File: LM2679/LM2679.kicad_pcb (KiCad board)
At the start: 2 copper layers, 61 x 35.6 mm, 15 parts, among them J1 - INPUT +, J2 + OUTPUT -, U1 LM2679SX-5.0/NOPB

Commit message: Updates to schematic and PCB
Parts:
- J1: value - INPUT + -> INPUT
- J2: value + OUTPUT - -> OUTPUT
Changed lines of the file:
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@@
   )
   (setup
-    (last_trace_width 1)
+    (last_trace_width 0.25)
     (user_trace_width 0.1)
     (user_trace_width 0.2)
@@
     (add_net "Net-(R1-Pad1)")
   )
+  (module Inductor_SMD:L_Bourns_SRP1245A (layer Front)
+    (at 154.686 83.058)
+    (descr "Bourns SRP1245A series SMD inductor http://www.bourns.com/docs/Product-Datasheets/SRP1245A.pdf")
+    (tags "Bourns SRP1245A SMD inductor")
+    (attr smd)
+    (fp_text reference L1 (at 0 7.366) (layer F.SilkS)
+      (effects (font (size 1 1) (thickness 0.15)))
+    )
+    (fp_text value "10µH 10A" (at 0 1.016) (layer F.Fab)
+      (effects (font (size 1 1) (thickness 0.15)))
+    )
+    (fp_line (start 6.45 2.8) (end 6.45 5.7) (layer F.SilkS) (width 0.12))
+    (fp_line (start -6.45 2.8) (end -6.45 5.7) (layer F.SilkS) (width 0.12))
+    (fp_line (start 5.75 6.5) (end -5.75 6.5) (layer F.CrtYd) (width 0.05))
+    (fp_line (start -5.75 -6.5) (end 5.75 -6.5) (layer F.CrtYd) (width 0.05))
+    (fp_line (start 6.45 -5.7) (end 6.45 -2.8) (layer F.SilkS) (width 0.12))
+    (fp_line (start 5.75 6.4) (end -5.75 6.4) (layer F.SilkS) (width 0.12))
+    (fp_line (start -6.45 -5.75) (end -6.45 -2.8) (layer F.SilkS) (width 0.12))
+    (fp_line (start -5.75 -6.4) (end 5.75 -6.4) (layer F.SilkS) (width 0.12))
+    (fp_line (start 6.3 -5.7) (end 6.3 5.7) (layer F.Fab) (width 0.1))
+    (fp_line (start 5.75 6.25) (end -5.75 6.25) (layer F.Fab) (width 0.1))
+    (fp_line (start -6.3 -5.75) (end -6.3 5.7) (layer F.Fab) (width 0.1))
+    (fp_line (start -5.75 -6.25) (end 5.75 -6.25) (layer F.Fab) (width 0.1))
+    (fp_line (start 8.001 2.7568) (end 6.55 2.75) (layer F.CrtYd) (width 0.05))
+    (fp_line (start 8.001 -2.7432) (end 6.55 -2.75) (layer F.CrtYd) (width 0.05))
+    (fp_line (start 8.001 -2.7432) (end 8.001 2.7568) (layer F.CrtYd) (width 0.05))
+    (fp_line (start 6.55 -5.7) (end 6.55 -2.75) (layer F.CrtYd) (width 0.05))
+    (fp_line (start 6.55 2.75) (end 6.55 5.7) (layer F.CrtYd) (width 0.05))
+    (fp_line (start -7.9502 2.75) (end -7.9502 -2.75) (layer F.CrtYd) (width 0.05))
+    (fp_line (start -7.9502 2.75) (end -6.55 2.75) (layer F.CrtYd) (width 0.05))
+    (fp_line (start -6.55 -2.75) (end -6.55 -5.7) (layer F.CrtYd) (width 0.05))
+    (fp_line (start -6.55 5.7) (end -6.55 2.75) (layer F.CrtYd) (width 0.05))
+    (fp_line (start -7.9502 -2.75) (end -6.55 -2.75) (layer F.CrtYd) (width 0.05))
+    (fp_text user %R (at 0 -0.762) (layer F.Fab)
+      (effects (font (size 1 1) (thickness 0.15)))
+    )
+    (fp_arc (start -5.75 -5.7) (end -5.75 -6.25) (angle -90) (layer F.Fab) (width 0.1))
+    (fp_arc (start 5.75 -5.7) (end 6.3 -5.7) (angle -90) (layer F.Fab) (width 0.1))
+    (fp_arc (start 5.75 5.7) (end 5.75 6.25) (angle -90) (layer F.Fab) (width 0.1))
+    (fp_arc (start -5.75 5.7) (end -6.3 5.7) (angle -90) (layer F.Fab) (width 0.1))
+    (fp_arc (start -5.75 -5.7) (end -5.75 -6.4) (angle -90) (layer F.SilkS) (width 0.12))
+    (fp_arc (start -5.75 5.7) (end -6.45 5.7) (angle -90) (layer F.SilkS) (width 0.12))
+    (fp_arc (start 5.75 5.7) (end 5.75 6.4) (angle -90) (layer F.SilkS) (width 0.12))
+    (fp_arc (start 5.75 -5.7) (end 6.45 -5.7) (angle -90) (layer F.SilkS) (width 0.12))
+    (fp_arc (start -5.75 -5.7) (end -5.75 -6.5) (angle -90) (layer F.CrtYd) (width 0.05))
+    (fp_arc (start -5.75 5.7) (end -6.55 5.7) (angle -90) (layer F.CrtYd) (width 0.05))
+    (fp_arc (start 5.75 5.7) (end 5.75 6.5) (angle -90) (layer F.CrtYd) (width 0.05))
+    (fp_arc (start 5.75 -5.7) (end 6.55 -5.7) (angle -90) (layer F.CrtYd) (width 0.05))
+    (pad 1 smd rect (at -5.8928 0) (size 3.8 5) (layers Front F.Paste F.Mask)
+      (net 7 "Net-(C4-Pad1)"))
+    (pad 2 smd rect (at 5.8928 0) (size 3.8 5) (layers Front F.Paste F.Mask)
+      (net 2 +5V))
+    (model ${KISYS3DMOD}/Inductor_SMD.3dshapes/L_Bourns_SRP1245A.wrl
+      (at (xyz 0 0 0))
+      (scale (xyz 1 1 1))
+      (rotate (xyz 0 0 0))
+    )
+    (model "${KISYS3DMOD}/Coils_User/SRP1265A series.stp"
+      (offset (xyz 0 0 4.9))
+      (scale (xyz 1 1 1))
+      (rotate (xyz 180 0 0))
+    )
+  )
   (module Capacitor_SMD:CP_Elec_8.3x8.3_Panasonic_M (layer Front)
     (at 124.714 97.79 180)
@@
       (effects (font (size 1 1) (thickness 0.15)))
     )
-    (fp_text value "+ OUTPUT -" (at 0 6.35 90) (layer F.SilkS)
+    (fp_text value OUTPUT (at 0 6.35 90) (layer F.SilkS)
       (effects (font (size 1 1) (thickness 0.15)))
     )
@@
       (effects (font (size 1 1) (thickness 0.15)))
     )
-    (fp_text value "- INPUT +" (at 0 6.35) (layer F.SilkS)
+    (fp_text value INPUT (at 0 6.35) (layer F.SilkS)
       (effects (font (size 1 1) (thickness 0.15)))
     )
@@
     )
   )
-  (module Inductor_SMD:L_Bourns_SRP1245A (layer Front)
-    (at 154.686 83.058)
-    (descr "Bourns SRP1245A series SMD inductor http://www.bourns.com/docs/Product-Datasheets/SRP1245A.pdf")
-    (tags "Bourns SRP1245A SMD inductor")
-    (attr smd)
-    (fp_text reference L1 (at 0 7.366) (layer F.SilkS)
-      (effects (font (size 1 1) (thickness 0.15)))
-    )
-    (fp_text value "10µH 10A" (at 0 1.016) (layer F.Fab)
-      (effects (font (size 1 1) (thickness 0.15)))
-    )
-    (fp_line (start 6.45 2.8) (end 6.45 5.7) (layer F.SilkS) (width 0.12))
-    (fp_line (start -6.45 2.8) (end -6.45 5.7) (layer F.SilkS) (width 0.12))
-    (fp_line (start 5.75 6.5) (end -5.75 6.5) (layer F.CrtYd) (width 0.05))
-    (fp_line (start -5.75 -6.5) (end 5.75 -6.5) (layer F.CrtYd) (width 0.05))
-    (fp_line (start 6.45 -5.7) (end 6.45 -2.8) (layer F.SilkS) (width 0.12))
-    (fp_line (start 5.75 6.4) (end -5.75 6.4) (layer F.SilkS) (width 0.12))
-    (fp_line (start -6.45 -5.75) (end -6.45 -2.8) (layer F.SilkS) (width 0.12))
-    (fp_line (start -5.75 -6.4) (end 5.75 -6.4) (layer F.SilkS) (width 0.12))
-    (fp_line (start 6.3 -5.7) (end 6.3 5.7) (layer F.Fab) (width 0.1))
-    (fp_line (start 5.75 6.25) (end -5.75 6.25) (layer F.Fab) (width 0.1))
-    (fp_line (start -6.3 -5.75) (end -6.3 5.7) (layer F.Fab) (width 0.1))
-    (fp_line (start -5.75 -6.25) (end 5.75 -6.25) (layer F.Fab) (width 0.1))
-    (fp_line (start 7.35 2.75) (end 6.55 2.75) (layer F.CrtYd) (width 0.05))
-    (fp_line (start 7.35 -2.75) (end 6.55 -2.75) (layer F.CrtYd) (width 0.05))
-    (fp_line (start 7.35 -2.75) (end 7.35 2.75) (layer F.CrtYd) (width 0.05))
-    (fp_line (start 6.55 -5.7) (end 6.55 -2.75) (layer F.CrtYd) (width 0.05))
-    (fp_line (start 6.55 2.75) (end 6.55 5.7) (layer F.CrtYd) (width 0.05))
-    (fp_line (start -7.35 2.75) (end -7.35 -2.75) (layer F.CrtYd) (width 0.05))
-    (fp_line (start -7.35 2.75) (end -6.55 2.75) (layer F.CrtYd) (width 0.05))
-    (fp_line (start -6.55 -2.75) (end -6.55 -5.7) (layer F.CrtYd) (width 0.05))
-    (fp_line (start -6.55 5.7) (end -6.55 2.75) (layer F.CrtYd) (width 0.05))
-    (fp_line (start -7.35 -2.75) (end -6.55 -2.75) (layer F.CrtYd) (width 0.05))
-    (fp_text user %R (at 0 -0.762) (layer F.Fab)
-      (effects (font (size 1 1) (thickness 0.15)))
-    )
-    (fp_arc (start -5.75 -5.7) (end -5.75 -6.25) (angle -90) (layer F.Fab) (width 0.1))
-    (fp_arc (start 5.75 -5.7) (end 6.3 -5.7) (angle -90) (layer F.Fab) (width 0.1))
-    (fp_arc (start 5.75 5.7) (end 5.75 6.25) (angle -90) (layer F.Fab) (width 0.1))
-    (fp_arc (start -5.75 5.7) (end -6.3 5.7) (angle -90) (layer F.Fab) (width 0.1))
-    (fp_arc (start -5.75 -5.7) (end -5.75 -6.4) (angle -90) (layer F.SilkS) (width 0.12))
-    (fp_arc (start -5.75 5.7) (end -6.45 5.7) (angle -90) (layer F.SilkS) (width 0.12))
-    (fp_arc (start 5.75 5.7) (end 5.75 6.4) (angle -90) (layer F.SilkS) (width 0.12))
-    (fp_arc (start 5.75 -5.7) (end 6.45 -5.7) (angle -90) (layer F.SilkS) (width 0.12))
-    (fp_arc (start -5.75 -5.7) (end -5.75 -6.5) (angle -90) (layer F.CrtYd) (width 0.05))
-    (fp_arc (start -5.75 5.7) (end -6.55 5.7) (angle -90) (layer F.CrtYd) (width 0.05))
-    (fp_arc (start 5.75 5.7) (end 5.75 6.5) (angle -90) (layer F.CrtYd) (width 0.05))
-    (fp_arc (start 5.75 -5.7) (end 6.55 -5.7) (angle -90) (layer F.CrtYd) (width 0.05))
-    (pad 2 smd rect (at 5.55 0) (size 3.1 5) (layers Front F.Paste F.Mask)
-      (net 2 +5V))
-    (pad 1 smd rect (at -5.55 0) (size 3.1 5) (layers Front F.Paste F.Mask)
-      (net 7 "Net-(C4-Pad1)"))
-    (model ${KISYS3DMOD}/Inductor_SMD.3dshapes/L_Bourns_SRP1245A.wrl
-      (at (xyz 0 0 0))
-      (scale (xyz 1 1 1))
-      (rotate (xyz 0 0 0))
-    )
-    (model "${KISYS3DMOD}/Coils_User/SRP1265A series.stp"
-      (offset (xyz 0 0 4.9))
-      (scale (xyz 1 1 1))
-      (rotate (xyz 180 0 0))
-    )
-  )

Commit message: Add Schematic and Images
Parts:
- J1: value INPUT -> - 12V.IN +
- J2: value OUTPUT -> + 5V.OUT -
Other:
- board text added: "BUCK REGULATOR V0.0.1"
- board text removed: "Buck Regulator V0.1.1"
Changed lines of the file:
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@@
     (44 Edge.Cuts user)
     (45 Margin user)
-    (46 B.CrtYd user hide)
-    (47 F.CrtYd user)
-    (49 F.Fab user)
+    (46 B.CrtYd user)
+    (47 F.CrtYd user hide)
+    (49 F.Fab user hide)
   )
   (setup
@@
     (user_trace_width 1)
     (trace_clearance 0.2)
-    (zone_clearance 0.3)
+    (zone_clearance 0.254)
     (zone_45_only no)
     (trace_min 0.1)
@@
     (pad_to_mask_clearance 0)
     (solder_mask_min_width 0.1)
-    (aux_axis_origin 117.856 75.438)
-    (grid_origin 117.856 75.438)
+    (aux_axis_origin 115.316 72.898)
+    (grid_origin 115.316 72.898)
     (visible_elements FFFFFF7F)
     (pcbplotparams
@@
       (effects (font (size 1 1) (thickness 0.15)))
     )
-    (fp_text value OUTPUT (at 0 6.35 90) (layer F.SilkS)
+    (fp_text value "+ 5V.OUT -" (at 0 6.35 90) (layer F.SilkS)
       (effects (font (size 1 1) (thickness 0.15)))
     )
@@
       (effects (font (size 1 1) (thickness 0.15)))
     )
-    (fp_text value INPUT (at 0 6.35) (layer F.SilkS)
+    (fp_text value "- 12V.IN +" (at 0 6.35) (layer F.SilkS)
       (effects (font (size 1 1) (thickness 0.15)))
     )
@@
     )
   )
-  (gr_text "Buck Regulator\nV0.1.1" (at 161.798 77.724) (layer F.SilkS)
+  (gr_text "BUCK\nREGULATOR\nV0.0.1" (at 135.89 79.756) (layer F.SilkS)
     (effects (font (size 1.016 1.016) (thickness 0.1524)) (justify left))
   )
@@
   (segment (start 140.97 96.1044) (end 142.0784 96.1044) (width 0.5) (layer Front) (net 7))
   (zone (net 1) (net_name GND) (layer Front) (hatch edge 0.508)
-    (connect_pads (clearance 0.3))
+    (connect_pads (clearance 0.254))
     (min_thickness 0.254)
-    (fill yes (arc_segments 32) (thermal_gap 0.254) (thermal_bridge_width 0.508) (smoothing fillet) (radius 1))
+    (fill yes (arc_segments 32) (thermal_gap 0.254) (thermal_bridge_width 0.508))
     (polygon
       (pts
@@
   )
   (zone (net 7) (net_name "Net-(C4-Pad1)") (layer Front) (hatch edge 0.508)
-    (connect_pads (clearance 0.3))
+    (connect_pads (clearance 0.254))
     (min_thickness 0.254)
-    (fill yes (arc_segments 32) (thermal_gap 0.254) (thermal_bridge_width 0.508) (smoothing fillet) (radius 1))
+    (fill yes (arc_segments 32) (thermal_gap 0.254) (thermal_bridge_width 0.508))
     (polygon
       (pts
@@
   )
   (zone (net 2) (net_name +5V) (layer Front) (hatch edge 0.508)
-    (connect_pads (clearance 0.3))
+    (connect_pads (clearance 0.254))
     (min_thickness 0.254)
-    (fill yes (arc_segments 32) (thermal_gap 0.254) (thermal_bridge_width 0.508) (smoothing fillet) (radius 1))
+    (fill yes (arc_segments 32) (thermal_gap 0.254) (thermal_bridge_width 0.508))
     (polygon
       (pts
@@
   )
   (zone (net 1) (net_name GND) (layer Back) (hatch edge 0.508)
-    (connect_pads (clearance 0.3))
+    (connect_pads (clearance 0.254))
     (min_thickness 0.254)
-    (fill yes (arc_segments 32) (thermal_gap 0.254) (thermal_bridge_width 0.508) (smoothing fillet) (radius 1))
+    (fill yes (arc_segments 32) (thermal_gap 0.254) (thermal_bridge_width 0.508))
     (polygon
       (pts
@@
   )
   (zone (net 3) (net_name +12V) (layer Front) (hatch edge 0.508)
-    (connect_pads (clearance 0.3))
+    (connect_pads (clearance 0.254))
     (min_thickness 0.254)
-    (fill yes (arc_segments 32) (thermal_gap 0.254) (thermal_bridge_width 0.508) (smoothing fillet) (radius 1))
+    (fill yes (arc_segments 32) (thermal_gap 0.254) (thermal_bridge_width 0.508))
     (polygon
       (pts

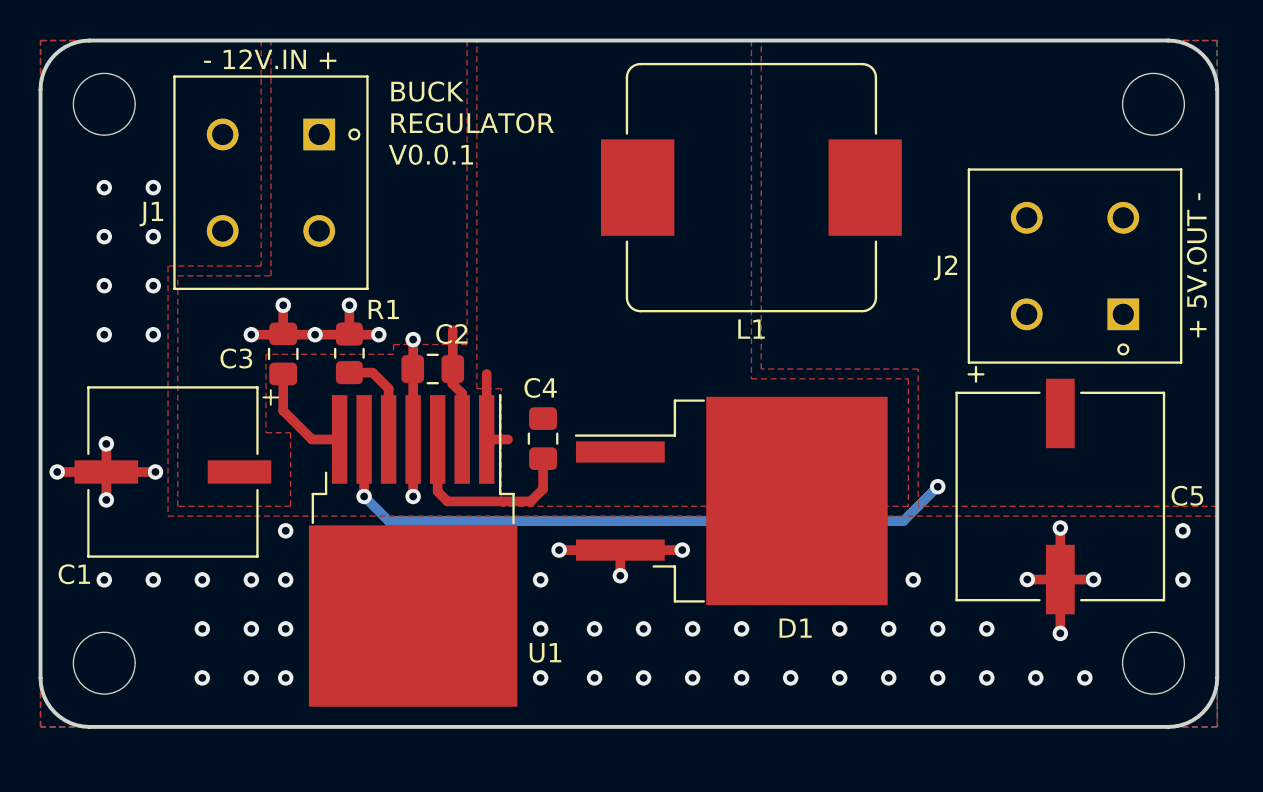
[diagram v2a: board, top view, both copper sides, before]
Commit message: Changes to PCB footprints
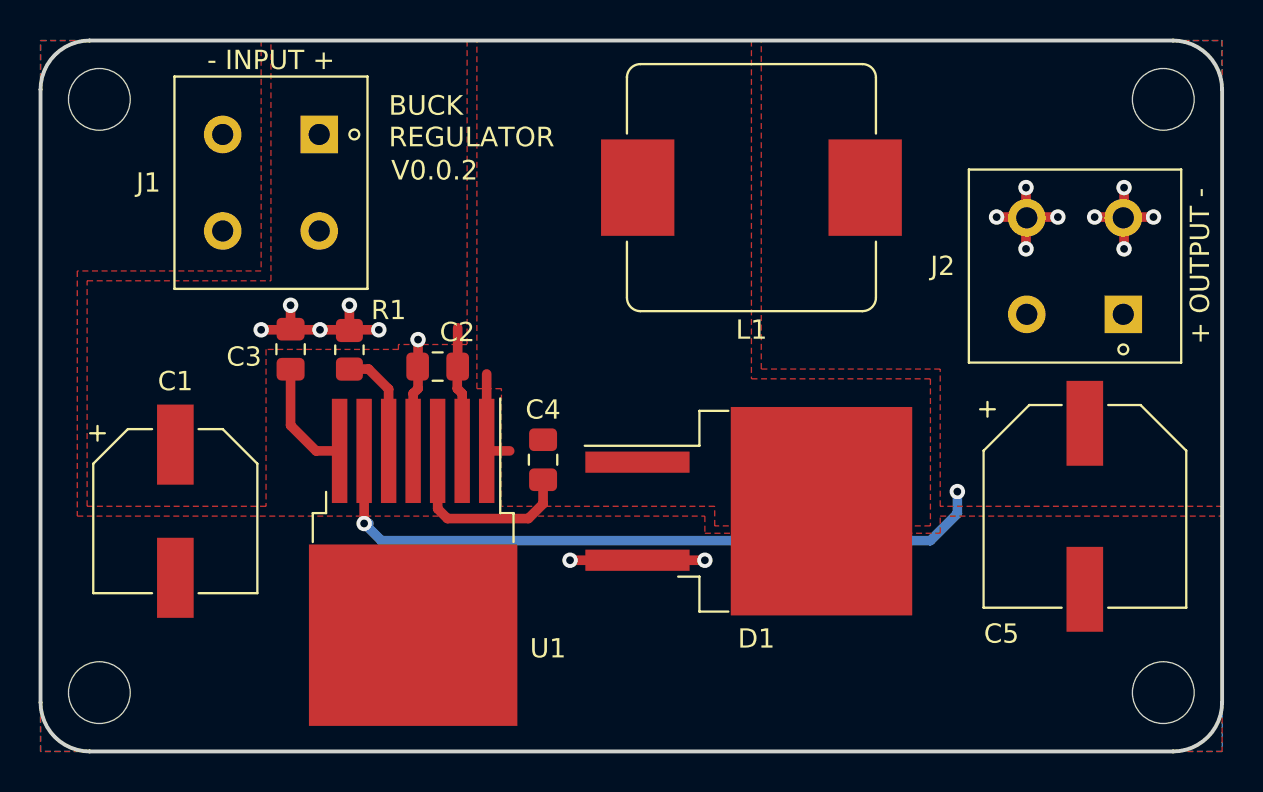
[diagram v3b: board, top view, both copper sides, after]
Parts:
- C1: footprint Capacitor_SMD:CP_Elec_8.3x8.3_Panasonic_M -> Capacitor_SMD:CP_Elec_8.3x8.3_Panasonic_SVPF_E7
- C5: footprint Capacitor_SMD:CP_Elec_10.3x10.3_Panasonic_M -> Capacitor_SMD:CP_Elec_10.3x10.3_Panasonic_SVPF_F12
- D1: footprint Package_TO_SOT_SMD:TO-263-2_TabPin1 -> Package_TO_SOT_SMD:TO-263-2_TabPin1_HandSoldering
- J1: value - 12V.IN + -> - INPUT +
- J2: value + 5V.OUT - -> + OUTPUT -
- U1: footprint Package_TO_SOT_SMD:TO-263-7_TabPin8 -> Package_TO_SOT_SMD:TO-263-7_TabPin8_HandSoldering
- moved C1 2.04 mm to (124.8, 99.8), turned to 270 degrees
- moved H3 1.61 mm to (176.0, 109.2)
- moved H4 1.55 mm to (120.9, 109.2)
- moved D1 1.38 mm to (154.9, 99.8)
- moved C5 1.37 mm to (172.0, 99.6)
- moved C4 1.09 mm to (143.9, 97.2)
- moved U1 0.99 mm to (137.2, 102.9)
- moved H2 0.57 mm to (176.0, 78.5)
- moved C3 0.45 mm to (130.8, 91.4)
- moved H1 0.36 mm to (120.9, 78.5)
- moved C2 0.28 mm to (138.4, 92.3)
- moved R1 0.18 mm to (133.9, 91.5)
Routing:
- net GND: track 42.4 -> 34.2 mm, vias 63 -> 16
- net +5V: track 33.9 -> 36.6 mm
- net Net-(C4-Pad1): track 4.50 -> 5.18 mm
- net Net-(R1-Pad1): track 5.01 -> 5.66 mm
- net +12V: track 5.88 -> 6.49 mm
- net Net-(C3-Pad1): track 5.44 -> 6.00 mm
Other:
- board size 61 x 35.6 mm -> 61.2 x 36.8 mm
- board text added: "BUCK REGULATOR"
- board text added: "V0.0.2"
- board text removed: "BUCK REGULATOR V0.0.1"

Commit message: Added vias to PCB
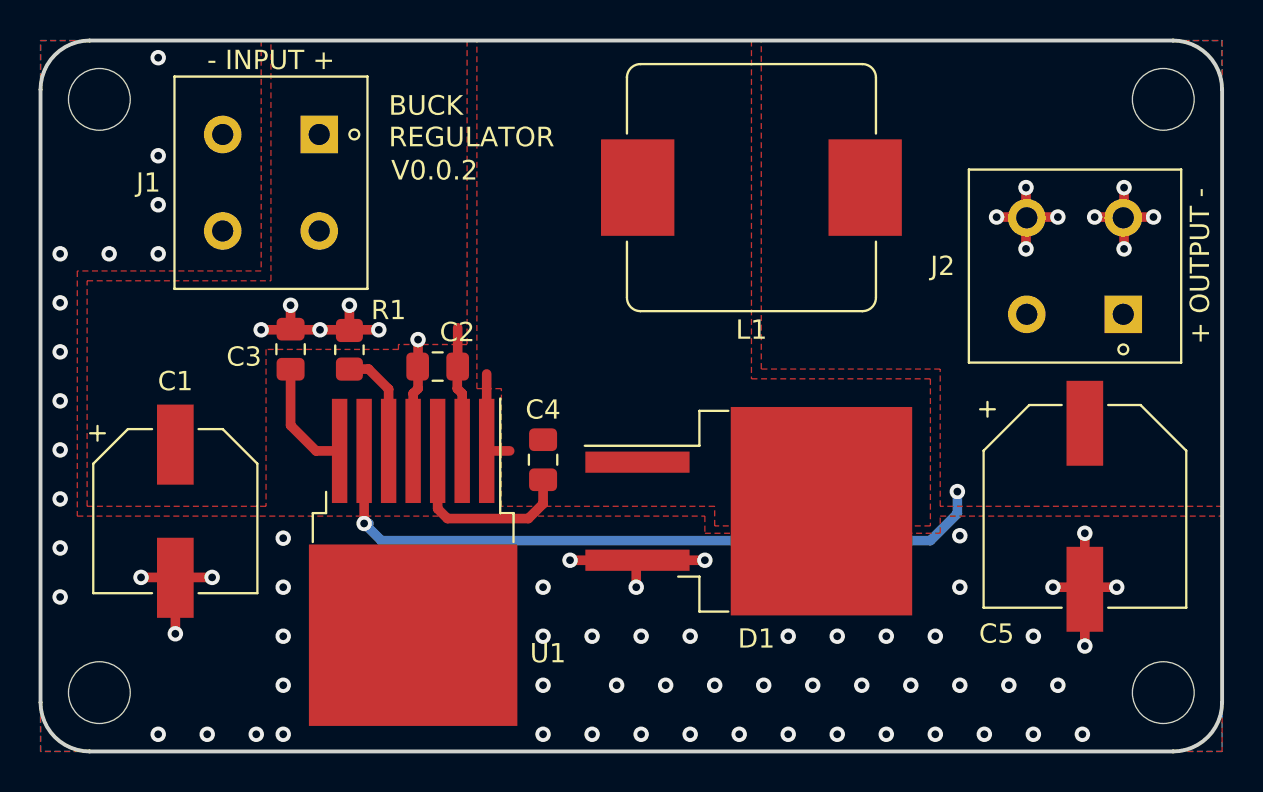
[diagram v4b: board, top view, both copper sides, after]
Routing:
- net GND: track 34.2 -> 51.4 mm, vias 16 -> 80
